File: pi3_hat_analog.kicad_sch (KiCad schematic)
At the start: 30 parts, among them J1 1935161, J3 Raspberry_Pi_2_3, J4 SJ1-3533NG, J5 SJ1-3533NG, J6 SJ1-3533NG, J7 SJ1-3533NG, Q1 2N3904BU, U1 MAX31856, U2 MCP3564RT, U3 MAX31856

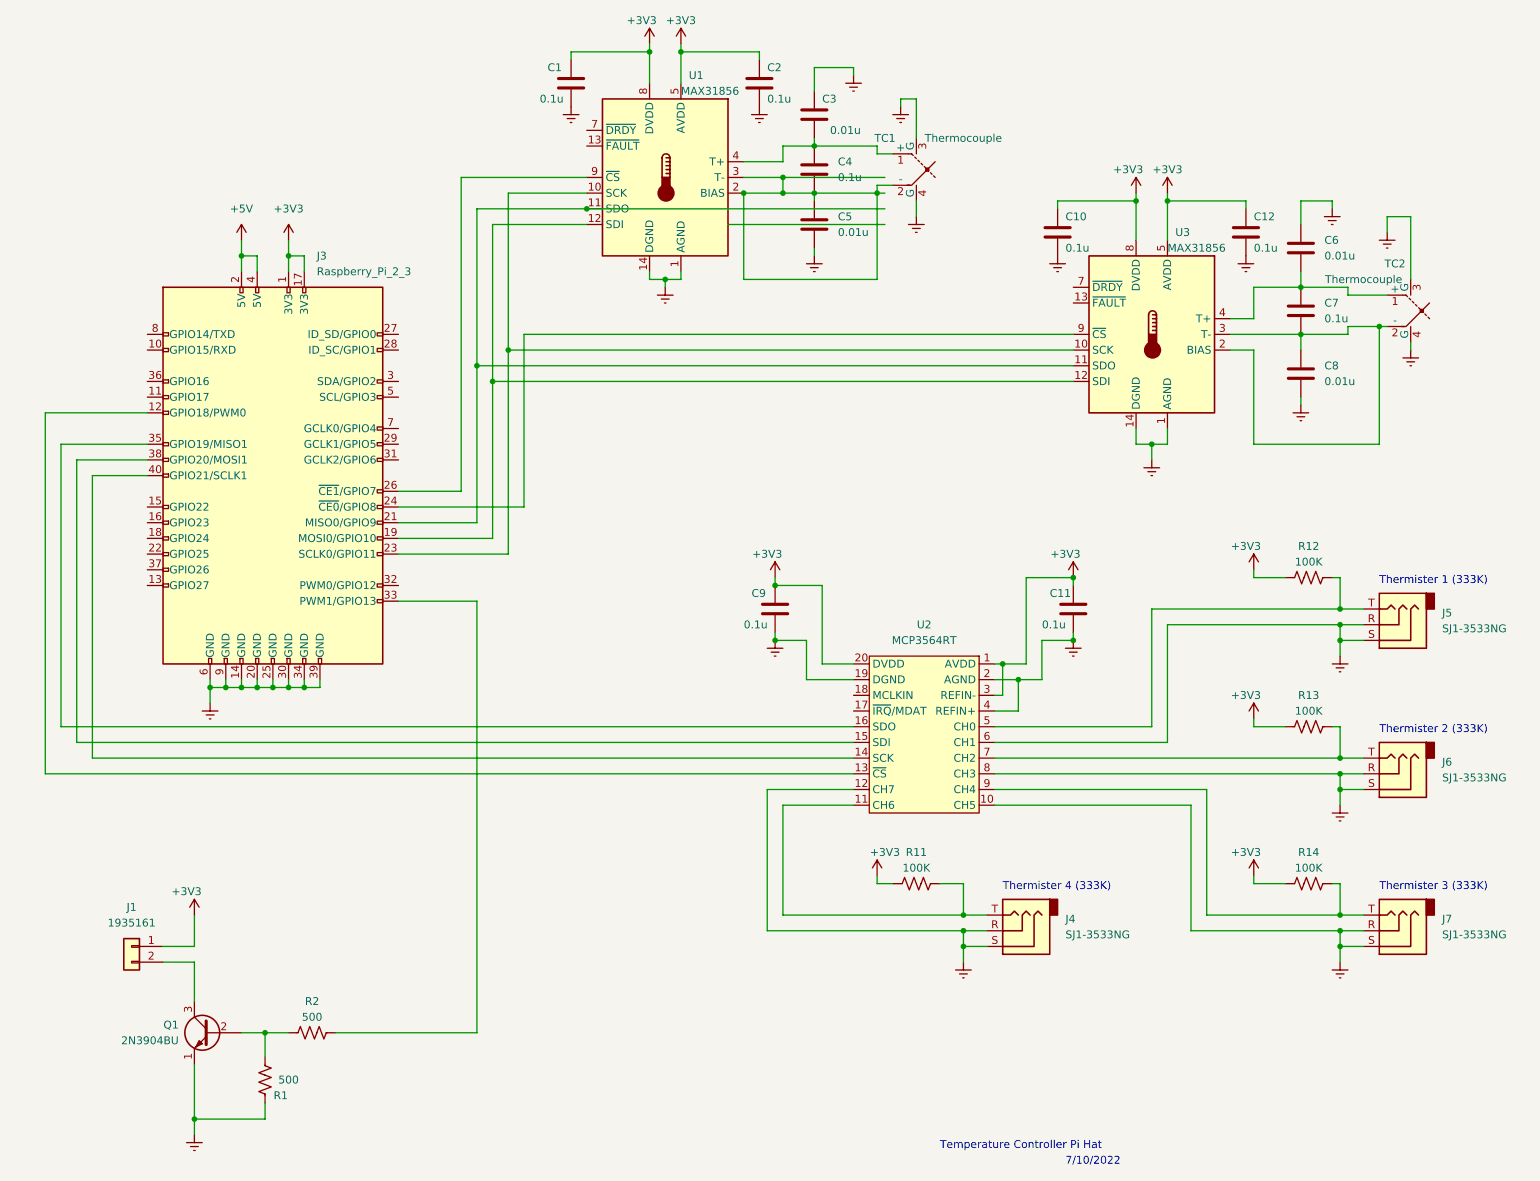
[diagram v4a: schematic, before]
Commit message: added leds
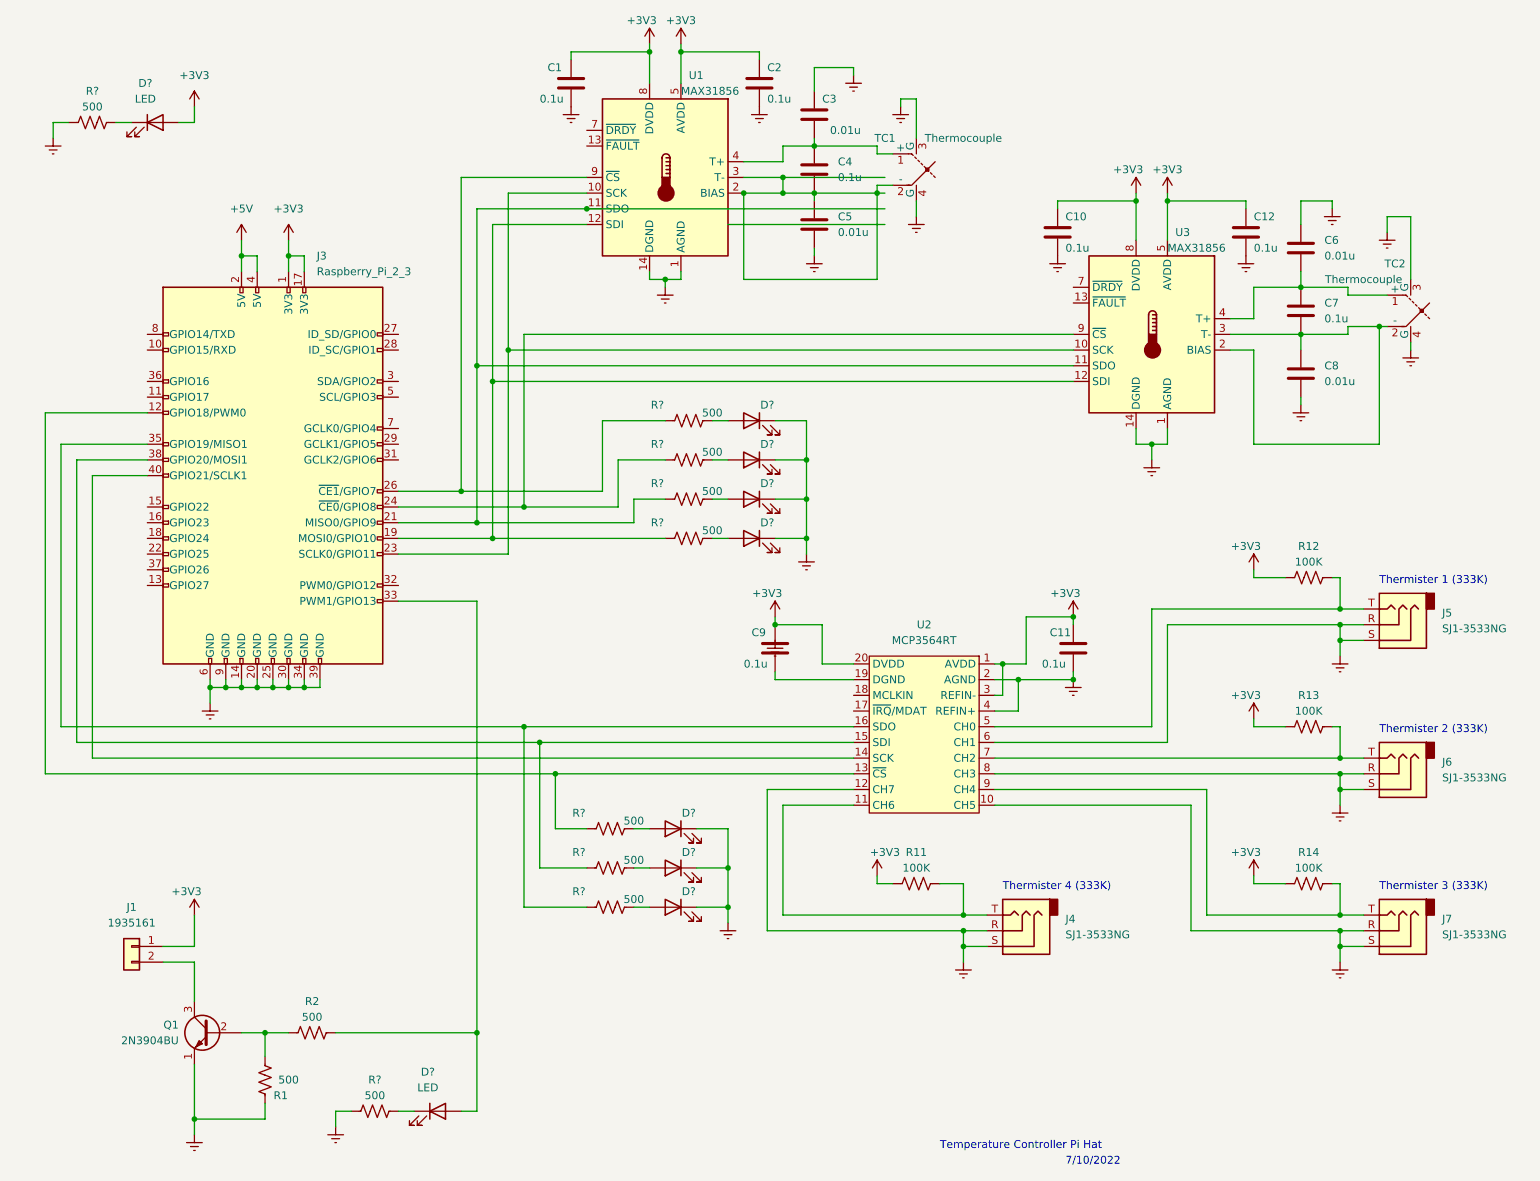
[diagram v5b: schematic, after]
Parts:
- added D? (x9): LED, symbol Device:LED
- added R? (x9): 500, Resistor_SMD:R_0201_0603Metric_Pad0.64x0.40mm_HandSolder, symbol Device:R_US
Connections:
- net +3V3: now also D?.2 (A)
- net GNDREF: now also D?.1 (K), D?.1 (K), D?.1 (K), D?.1 (K), D?.1 (K), D?.1 (K), D?.1 (K), R?.1, R?.1; no longer C9.2, U2.19 (DGND)
- net at J3.12 (GPIO18/PWM0), U2.13 (~{CS}): now also R?.1
- net at J3.19 (MOSI0/GPIO10), U1.12 (SDI), U3.12 (SDI): now also R?.1
- net at J3.21 (MISO0/GPIO9), U1.11 (SDO), U3.11 (SDO): now also R?.1
- net at J3.24 (~{CE0}/GPIO8), U3.9 (~{CS}): now also R?.1
- net at J3.26 (~{CE1}/GPIO7), U1.9 (~{CS}): now also R?.1
- net at J3.33 (PWM1/GPIO13), R2.2: now also D?.2 (A)
- net at J3.35 (GPIO19/MISO1), U2.16 (SDO): now also R?.1
- net at J3.38 (GPIO20/MOSI1), U2.15 (SDI): now also R?.1
- new net: D?.2 (A), R?.2 (x7)
- new net: D?.1 (K), R?.2 (x2)
- new net: C9.2, U2.19 (DGND)
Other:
- moved on the sheet: C11, C9

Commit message: more placement
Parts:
- D1, D2, D3, D4, D5, D6, D7, D8, D9: renamed from D?; footprint (none) -> LED_SMD:LED_0603_1608Metric_Pad1.05x0.95mm_HandSolder
- R1, R11, R12, R13, R14, R2: footprint Resistor_SMD:R_0201_0603Metric_Pad0.64x0.40mm_HandSolder -> Resistor_SMD:R_0603_1608Metric_Pad0.98x0.95mm_HandSolder
- R10, R15, R3, R4, R5, R6, R7, R8, R9: renamed from R?; footprint Resistor_SMD:R_0201_0603Metric_Pad0.64x0.40mm_HandSolder -> Resistor_SMD:R_0603_1608Metric_Pad0.98x0.95mm_HandSolder
